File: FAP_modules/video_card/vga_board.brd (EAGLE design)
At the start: 100 x 75 mm, 32 parts, among them IC1 IS61LV256, IC2 IS61LV256

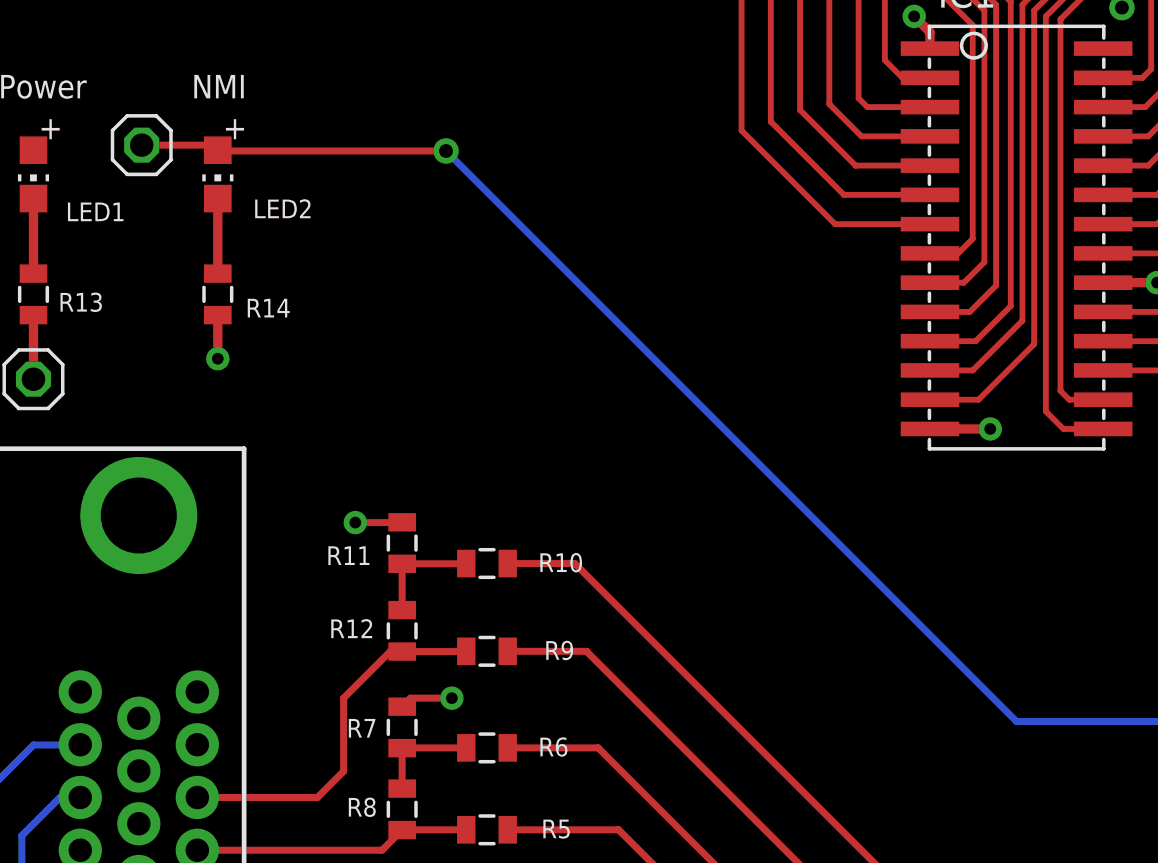
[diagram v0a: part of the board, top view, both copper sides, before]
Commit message: vga pcb trace fix
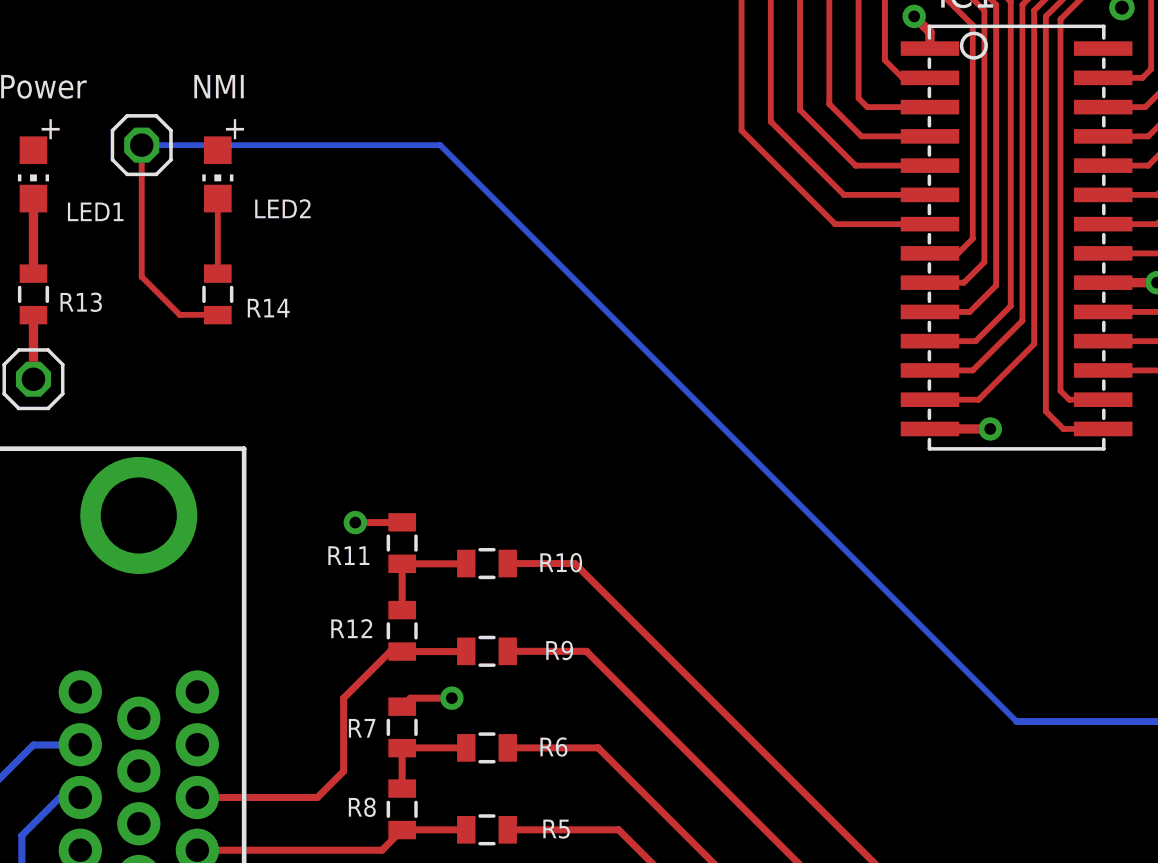
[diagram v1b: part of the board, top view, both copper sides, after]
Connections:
- net +3V3: now also LED2.A
- net GND: no longer R14.1
- net N$36: now also R14.1; no longer LED2.A
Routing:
- net N$36: track 95.8 -> 105.5 mm, vias 1 -> 0
- net GND: track 35.9 -> 34.0 mm, vias 14 -> 13
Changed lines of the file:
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@@
 <setting verticaltext="up"/>
 </settings>
-<grid distance="10" unitdist="mil" unit="mil" style="lines" multiple="1" display="no" altdistance="1" altunitdist="mil" altunit="mil"/>
+<grid distance="1" unitdist="mil" unit="mil" style="lines" multiple="1" display="no" altdistance="1" altunitdist="mil" altunit="mil"/>
 <layers>
 <layer number="1" name="Top" color="4" fill="1" visible="yes" active="yes"/>
@@
 <wire x1="56.134" y1="44.196" x2="58.544" y2="44.196" width="0.4064" layer="1"/>
 <contactref element="R13" pad="1"/>
-<contactref element="R14" pad="1"/>
-<via x="11.557" y="45.974" extent="1-16" drill="0.508"/>
-<wire x1="11.557" y1="45.974" x2="11.557" y2="47.868" width="0.4064" layer="1"/>
 <wire x1="63.881" y1="52.324" x2="65.9892" y2="52.324" width="0.4064" layer="1"/>
 <wire x1="65.9892" y1="52.324" x2="66.04" y2="52.2732" width="0.3048" layer="1"/>
@@
 <contactref element="R17" pad="2"/>
 <contactref element="R18" pad="2"/>
+<contactref element="LED2" pad="A"/>
 </signal>
 <signal name="+5V">
@@
 <wire x1="3.556" y1="52.925" x2="3.556" y2="49.668" width="0.4064" layer="1"/>
 </signal>
-<signal name="N$35">
-<contactref element="LED2" pad="C"/>
-<contactref element="R14" pad="2"/>
-<wire x1="11.557" y1="49.668" x2="11.557" y2="52.925" width="0.4064" layer="1"/>
-</signal>
 <signal name="N$36">
 <contactref element="U$3" pad="142"/>
-<contactref element="LED2" pad="A"/>
 <wire x1="72.39" y1="12.7" x2="71.12" y2="13.97" width="0.3048" layer="16"/>
 <wire x1="71.12" y1="13.97" x2="71.12" y2="21.082" width="0.3048" layer="16"/>
 <wire x1="71.12" y1="21.082" x2="61.976" y2="30.226" width="0.3048" layer="16"/>
 <wire x1="61.976" y1="30.226" x2="46.228" y2="30.226" width="0.3048" layer="16"/>
-<wire x1="46.228" y1="30.226" x2="21.463" y2="54.991" width="0.3048" layer="16"/>
-<via x="21.463" y="54.991" extent="1-16" drill="0.6"/>
-<wire x1="21.463" y1="54.991" x2="11.591" y2="54.991" width="0.3048" layer="1"/>
-<wire x1="11.591" y1="54.991" x2="11.557" y2="55.025" width="0.3048" layer="1"/>
 <contactref element="JP1" pad="1"/>
-<wire x1="8.255" y1="55.245" x2="11.337" y2="55.245" width="0.3048" layer="1"/>
-<wire x1="11.337" y1="55.245" x2="11.557" y2="55.025" width="0.3048" layer="1"/>
 <contactref element="U$1" pad="NMI"/>
 <wire x1="76.708" y1="4.572" x2="76.708" y2="8.382" width="0.254" layer="16"/>
 <wire x1="76.708" y1="8.382" x2="72.39" y2="12.7" width="0.254" layer="16"/>
+<wire x1="46.228" y1="30.226" x2="21.209" y2="55.245" width="0.254" layer="16"/>
+<wire x1="21.209" y1="55.245" x2="8.255" y2="55.245" width="0.254" layer="16"/>
+<contactref element="R14" pad="1"/>
+<wire x1="8.255" y1="55.245" x2="8.255" y2="49.53" width="0.254" layer="1"/>
+<wire x1="8.255" y1="49.53" x2="9.906" y2="47.879" width="0.254" layer="1"/>
+<wire x1="9.906" y1="47.879" x2="11.546" y2="47.879" width="0.254" layer="1"/>
+<wire x1="11.546" y1="47.879" x2="11.557" y2="47.868" width="0.254" layer="1"/>
 </signal>
 <signal name="N$37">
@@
 <wire x1="96.266" y1="57.404" x2="87.63" y2="66.04" width="0.3048" layer="16"/>
 </signal>
+<signal name="N$35">
+<contactref element="LED2" pad="C"/>
+<contactref element="R14" pad="2"/>
+<wire x1="11.557" y1="49.668" x2="11.557" y2="52.925" width="0.254" layer="1"/>
+</signal>
 </signals>
